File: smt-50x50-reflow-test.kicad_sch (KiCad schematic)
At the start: 86 parts, among them J1 Conn_01x04_Pin, J2 Conn_01x02, J4 USB_C_Receptacle_USB2.0_14P, J8 Conn_01x04_Pin, J9 Conn_01x03_Pin, SW1 SW_Push, SW2 SW_Push, U1 ESP32-C6, U14 TMP117AIDRV, U15 BMP581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

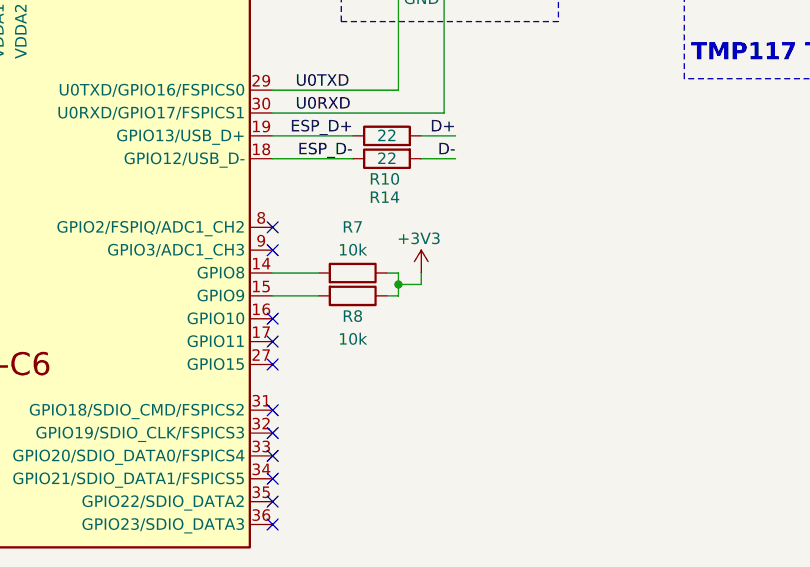
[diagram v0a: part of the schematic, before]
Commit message: schem: add missing i2c net labels
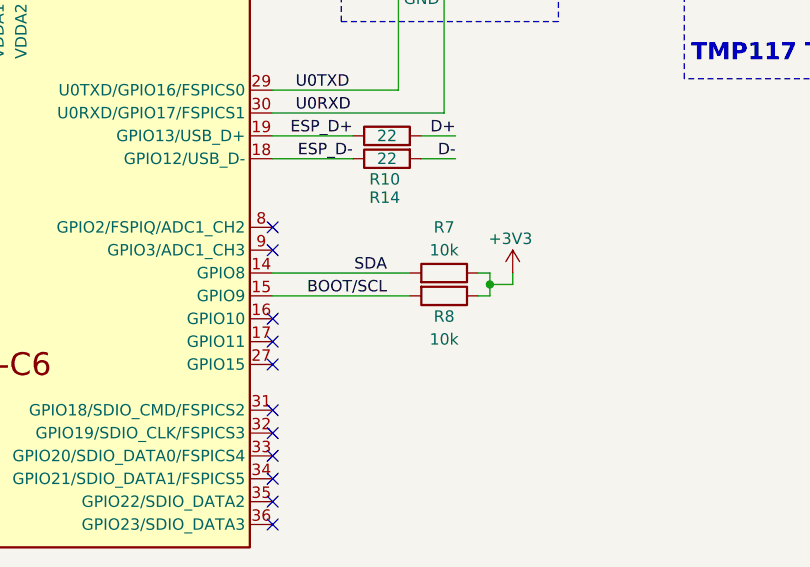
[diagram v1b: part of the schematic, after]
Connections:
- net BOOT/SCL: now also R8.2, U1.15 (GPIO9)
- net SDA: now also R7.2, U1.14 (GPIO8)
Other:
- moved on the sheet: R7, R8
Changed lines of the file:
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@@
 	)
 	(junction
-		(at 152.4 80.01)
+		(at 162.56 80.01)
 		(diameter 0)
 		(color 0 0 0 0)
@@
 	(wire
 		(pts
-			(xy 152.4 81.28) (xy 152.4 80.01)
+			(xy 162.56 81.28) (xy 162.56 80.01)
 		)
 		(stroke
@@
 	(wire
 		(pts
-			(xy 151.13 81.28) (xy 152.4 81.28)
+			(xy 161.29 81.28) (xy 162.56 81.28)
 		)
 		(stroke
@@
 	(wire
 		(pts
-			(xy 152.4 80.01) (xy 152.4 78.74)
+			(xy 162.56 80.01) (xy 162.56 78.74)
 		)
 		(stroke
@@
 	(wire
 		(pts
-			(xy 152.4 78.74) (xy 151.13 78.74)
+			(xy 162.56 78.74) (xy 161.29 78.74)
 		)
 		(stroke
@@
 	(wire
 		(pts
-			(xy 152.4 80.01) (xy 154.94 80.01)
+			(xy 162.56 80.01) (xy 165.1 80.01)
 		)
 		(stroke
@@
 	(wire
 		(pts
-			(xy 138.43 81.28) (xy 143.51 81.28)
+			(xy 138.43 81.28) (xy 153.67 81.28)
 		)
 		(stroke
@@
 	(wire
 		(pts
+			(xy 138.43 78.74) (xy 153.67 78.74)
+		)
+		(stroke
+			(width 0)
+			(type default)
+		)
+	)
+	(wire
+		(pts
 			(xy 41.91 158.75) (xy 44.45 158.75)
 		)
@@
 	(wire
 		(pts
-			(xy 154.94 80.01) (xy 154.94 78.74)
+			(xy 165.1 80.01) (xy 165.1 78.74)
 		)
 		(stroke
@@
 	(wire
 		(pts
-			(xy 143.51 78.74) (xy 138.43 78.74)
-		)
-		(stroke
-			(width 0)
-			(type default)
-		)
-	)
-	(wire
-		(pts
 			(xy 90.17 33.02) (xy 80.01 33.02)
 		)
@@
 		)
 	)
+	(label "BOOT{slash}SCL"
+		(at 151.13 81.28 180)
+		(effects
+			(font
+				(size 1.27 1.27)
+			)
+			(justify right bottom)
+		)
+	)
 	(label "XTAL_P"
 		(at 50.8 180.34 0)
@@
 		)
 	)
+	(label "SDA"
+		(at 151.13 78.74 180)
+		(effects
+			(font
+				(size 1.27 1.27)
+			)
+			(justify right bottom)
+		)
+	)
 	(label "U0RXD"
 		(at 140.97 60.96 0)
@@
 	(symbol
 		(lib_id "power:+3V3")
-		(at 154.94 78.74 0)
+		(at 165.1 78.74 0)
 		(unit 1)
 		(exclude_from_sim no)
@@
 		(dnp no)
 		(property "Reference" "#PWR03"
-			(at 154.94 82.55 0)
+			(at 165.1 82.55 0)
 			(effects
 				(font
@@
 		)
 		(property "Value" "+3V3"
-			(at 154.686 74.93 0)
+			(at 164.846 74.93 0)
 			(effects
 				(font
@@
 		)
 		(property "Footprint" ""
-			(at 154.94 78.74 0)
+			(at 165.1 78.74 0)
 			(effects
 				(font
@@
 		)
 		(property "Datasheet" ""
-			(at 154.94 78.74 0)
+			(at 165.1 78.74 0)
 			(effects
 				(font
@@
 		)
 		(property "Description" "Power symbol creates a global label with name \"+3V3\""
-			(at 154.94 78.74 0)
+			(at 165.1 78.74 0)
 			(effects
 				(font
@@
 	(symbol
 		(lib_id "Device:R")
-		(at 147.32 81.28 270)
+		(at 157.48 81.28 270)
 		(unit 1)
 		(exclude_from_sim no)
@@
 		(dnp no)
 		(property "Reference" "R8"
-			(at 147.32 83.566 90)
+			(at 157.48 83.566 90)
 			(effects
 				(font
@@
 		)
 		(property "Value" "10k"
-			(at 147.32 86.106 90)
+			(at 157.48 86.106 90)
 			(effects
 				(font
@@
 		)
 		(property "Footprint" ""
-			(at 147.32 79.502 90)
+			(at 157.48 79.502 90)
 			(effects
 				(font
@@
 		)
 		(property "Datasheet" "~"
-			(at 147.32 81.28 0)
+			(at 157.48 81.28 0)
 			(effects
 				(font
@@
 		)
 		(property "Description" "Resistor"
-			(at 147.32 81.28 0)
+			(at 157.48 81.28 0)
 			(effects
 				(font
@@
 	(symbol
 		(lib_id "Device:R")
-		(at 147.32 78.74 270)
+		(at 157.48 78.74 270)
 		(mirror x)
 		(unit 1)
@@
 		(dnp no)
 		(property "Reference" "R7"
-			(at 147.32 73.66 90)
+			(at 157.48 73.66 90)
 			(effects
 				(font
@@
 		)
 		(property "Value" "10k"
-			(at 147.32 76.2 90)
+			(at 157.48 76.2 90)
 			(effects
 				(font
@@
 		)
 		(property "Footprint" ""
-			(at 147.32 80.518 90)
+			(at 157.48 80.518 90)
 			(effects
 				(font
@@
 		)
 		(property "Datasheet" "~"
-			(at 147.32 78.74 0)
+			(at 157.48 78.74 0)
 			(effects
 				(font
@@
 		)
 		(property "Description" "Resistor"
-			(at 147.32 78.74 0)
+			(at 157.48 78.74 0)
 			(effects
 				(font

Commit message: schem: add missing footprints
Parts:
- J2: footprint (none) -> Connector_PinHeader_2.54mm:PinHeader_1x02_P2.54mm_Vertical
- R7, R8: footprint (none) -> Resistor_SMD:R_0402_1005Metric
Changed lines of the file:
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@@
 			)
 		)
-		(property "Footprint" ""
+		(property "Footprint" "Connector_PinHeader_2.54mm:PinHeader_1x02_P2.54mm_Vertical"
 			(at 187.96 134.62 0)
 			(effects
@@
 			)
 		)
-		(property "Footprint" ""
+		(property "Footprint" "Resistor_SMD:R_0402_1005Metric"
 			(at 157.48 79.502 90)
 			(effects
@@
 			)
 		)
-		(property "Footprint" ""
+		(property "Footprint" "Resistor_SMD:R_0402_1005Metric"
 			(at 157.48 80.518 90)
 			(effects

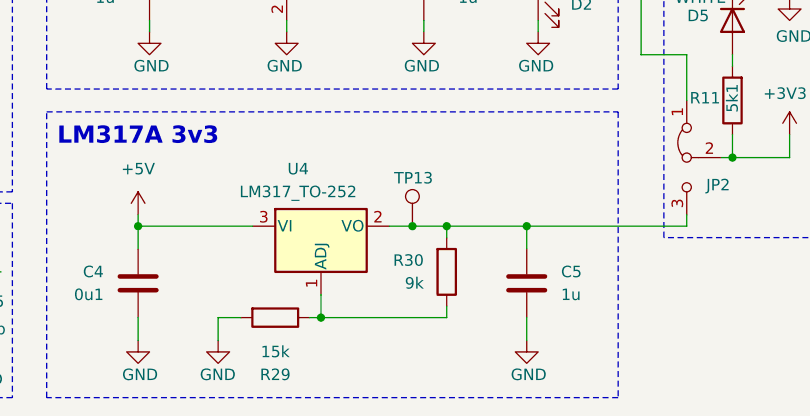
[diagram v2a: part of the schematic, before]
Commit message: schem: add ordering info to BOM
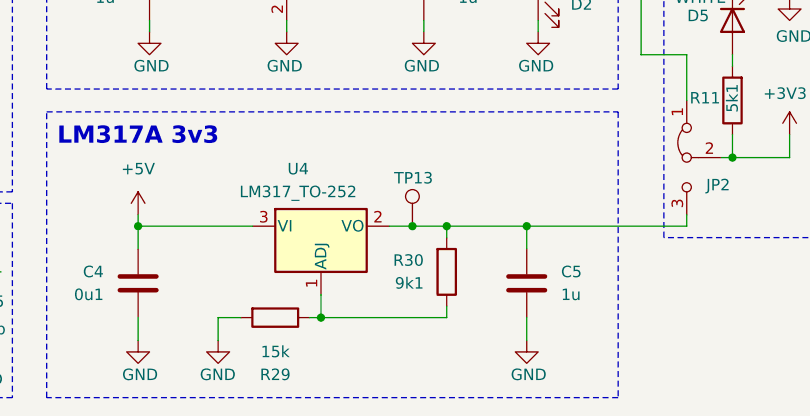
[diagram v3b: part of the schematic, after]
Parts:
- J2: now left out of the parts list
- L2, L4: JLCPCB Part # C412269 -> C77108; Manufacturer Part Number LQW15AN2N7G80D -> LQG15HS2N7S02D
- R29: JLCPCB Part # (none) -> C22809; Manufacturer (none) -> Uniroyal Elec; Manufacturer Part Number (none) -> 0603WAF1502T5E
- R30: value 9k -> 9k1; JLCPCB Part # (none) -> C23260; Manufacturer (none) -> Uniroyal Elec; Manufacturer Part Number (none) -> 0603WAF9101T5E
- R7, R8: JLCPCB Part # (none) -> C25744; Manufacturer (none) -> Uniroyal Elec; Manufacturer Part Number (none) -> 0402WGF1002TCE
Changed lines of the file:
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@@
 		(unit 1)
 		(exclude_from_sim no)
-		(in_bom yes)
+		(in_bom no)
 		(on_board yes)
 		(dnp no)
@@
 			)
 		)
-		(property "JLCPCB Part #" ""
+		(property "JLCPCB Part #" "C22809"
 			(at 110.49 185.42 0)
 			(effects
@@
 			)
 		)
-		(property "Manufacturer" ""
+		(property "Manufacturer" "Uniroyal Elec"
 			(at 110.49 185.42 0)
 			(effects
@@
 			)
 		)
-		(property "Manufacturer Part Number" ""
+		(property "Manufacturer Part Number" "0603WAF1502T5E"
 			(at 110.49 185.42 0)
 			(effects
@@
 			)
 		)
-		(property "Manufacturer Part Number" "LQW15AN2N7G80D"
+		(property "Manufacturer Part Number" "LQG15HS2N7S02D"
 			(at 85.09 22.86 90)
 			(effects
@@
 			)
 		)
-		(property "JLCPCB Part #" "C412269"
+		(property "JLCPCB Part #" "C77108"
 			(at 85.09 22.86 90)
 			(effects
@@
 			)
 		)
+		(property "JLCPCB Part #" "C25744"
+			(at 157.48 81.28 90)
+			(effects
+				(font
+					(size 1.27 1.27)
+				)
+				(hide yes)
+			)
+		)
+		(property "Manufacturer" "Uniroyal Elec"
+			(at 157.48 81.28 90)
+			(effects
+				(font
+					(size 1.27 1.27)
+				)
+				(hide yes)
+			)
+		)
+		(property "Manufacturer Part Number" "0402WGF1002TCE"
+			(at 157.48 81.28 90)
+			(effects
+				(font
+					(size 1.27 1.27)
+				)
+				(hide yes)
+			)
+		)
 		(pin "1"
 		)
@@
 			)
 		)
+		(property "JLCPCB Part #" "C25744"
+			(at 157.48 78.74 90)
+			(effects
+				(font
+					(size 1.27 1.27)
+				)
+				(hide yes)
+			)
+		)
+		(property "Manufacturer" "Uniroyal Elec"
+			(at 157.48 78.74 90)
+			(effects
+				(font
+					(size 1.27 1.27)
+				)
+				(hide yes)
+			)
+		)
+		(property "Manufacturer Part Number" "0402WGF1002TCE"
+			(at 157.48 78.74 90)
+			(effects
+				(font
+					(size 1.27 1.27)
+				)
+				(hide yes)
+			)
+		)
 		(pin "1"
 		)
@@
 			)
 		)
-		(property "Manufacturer Part Number" "LQW15AN2N7G80D"
+		(property "Manufacturer Part Number" "LQG15HS2N7S02D"
 			(at 55.88 39.37 90)
 			(effects
@@
 			)
 		)
-		(property "JLCPCB Part #" "C412269"
+		(property "JLCPCB Part #" "C77108"
 			(at 55.88 39.37 90)
 			(effects
@@
 			)
 		)
-		(property "Value" "9k"
+		(property "Value" "9k1"
 			(at 127 181.6099 0)
 			(effects
@@
 			)
 		)
-		(property "JLCPCB Part #" ""
+		(property "JLCPCB Part #" "C23260"
 			(at 129.54 180.34 90)
 			(effects
@@
 			)
 		)
-		(property "Manufacturer" ""
+		(property "Manufacturer" "Uniroyal Elec"
 			(at 129.54 180.34 90)
 			(effects
@@
 			)
 		)
-		(property "Manufacturer Part Number" ""
+		(property "Manufacturer Part Number" "0603WAF9101T5E"
 			(at 129.54 180.34 90)
 			(effects

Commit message: schem: add title
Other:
- company: (none) -> Rémi Ait-Younes
- title: (none) -> SMT 50x50 reflow test
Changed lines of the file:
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@@
 	(generator_version "9.0")
 	(paper "A4")
+	(title_block
+		(title "SMT 50x50 reflow test")
+		(date "2025-11-15")
+		(rev "01")
+		(company "Rémi Ait-Younes")
+	)
 	(rectangle
 		(start 49.53 172.72)

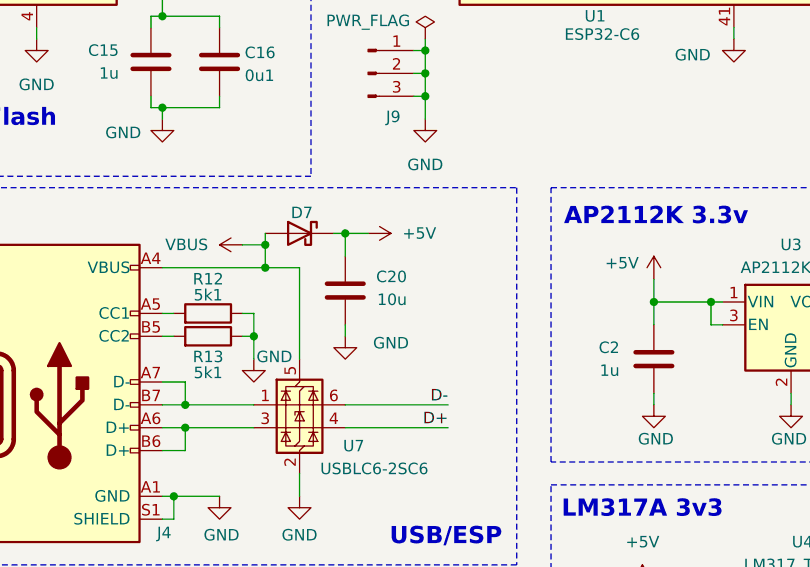
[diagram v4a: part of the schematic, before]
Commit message: schem: add esd protection to usb vbus
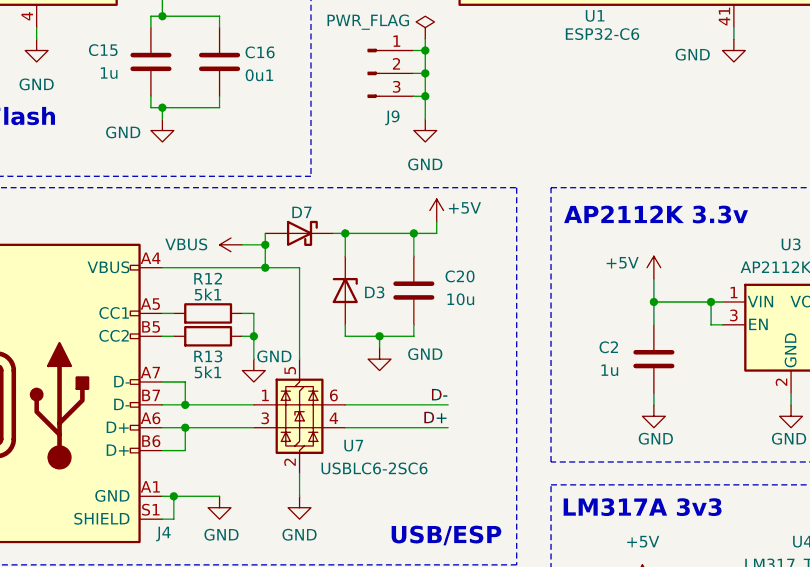
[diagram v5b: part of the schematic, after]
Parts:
- added D3: H5VU10U, Pers:Diode_DFN1006, symbol Pers:H5VU10U
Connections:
- net +5V: now also D3.1 (K)
- net GND: now also D3.2 (A)
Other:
- moved on the sheet: C20
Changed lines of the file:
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@@
 	)
 	(junction
-		(at 62.23 134.62)
+		(at 44.45 156.21)
 		(diameter 0)
 		(color 0 0 0 0)
 	)
 	(junction
-		(at 44.45 156.21)
+		(at 69.85 134.62)
 		(diameter 0)
 		(color 0 0 0 0)
@@
 	)
 	(junction
+		(at 66.04 146.05)
+		(diameter 0)
+		(color 0 0 0 0)
+	)
+	(junction
 		(at 102.87 142.24)
 		(diameter 0)
@@
 	)
 	(junction
+		(at 62.23 134.62)
+		(diameter 0)
+		(color 0 0 0 0)
+	)
+	(junction
 		(at 110.49 44.45)
 		(diameter 0)
@@
 	(wire
 		(pts
+			(xy 72.39 133.35) (xy 72.39 134.62)
+		)
+		(stroke
+			(width 0)
+			(type default)
+		)
+	)
+	(wire
+		(pts
 			(xy 139.7 152.4) (xy 139.7 153.67)
 		)
@@
 	(wire
 		(pts
-			(xy 62.23 134.62) (xy 60.96 134.62)
+			(xy 60.96 134.62) (xy 62.23 134.62)
 		)
 		(stroke
@@
 	(wire
 		(pts
-			(xy 64.77 134.62) (xy 62.23 134.62)
-		)
-		(stroke
-			(width 0)
-			(type default)
-		)
-	)
-	(wire
-		(pts
 			(xy 154.94 36.83) (xy 154.94 44.45)
 		)
@@
 	(wire
 		(pts
+			(xy 62.23 134.62) (xy 69.85 134.62)
+		)
+		(stroke
+			(width 0)
+			(type default)
+		)
+	)
+	(wire
+		(pts
 			(xy 49.53 39.37) (xy 52.07 39.37)
 		)
@@
 	(wire
 		(pts
-			(xy 62.23 146.05) (xy 62.23 144.78)
+			(xy 66.04 147.32) (xy 66.04 146.05)
 		)
 		(stroke
@@
 	(wire
 		(pts
+			(xy 66.04 146.05) (xy 69.85 146.05)
+		)
+		(stroke
+			(width 0)
+			(type default)
+		)
+	)
+	(wire
+		(pts
 			(xy 266.7 64.77) (xy 265.43 64.77)
 		)
@@
 	(wire
 		(pts
+			(xy 62.23 134.62) (xy 62.23 137.16)
+		)
+		(stroke
+			(width 0)
+			(type default)
+		)
+	)
+	(wire
+		(pts
 			(xy 129.54 175.26) (xy 138.43 175.26)
 		)
@@
 	(wire
 		(pts
-			(xy 62.23 134.62) (xy 62.23 137.16)
+			(xy 69.85 134.62) (xy 69.85 137.16)
 		)
 		(stroke
@@
 	(wire
 		(pts
+			(xy 62.23 146.05) (xy 62.23 144.78)
+		)
+		(stroke
+			(width 0)
+			(type default)
+		)
+	)
+	(wire
+		(pts
 			(xy 156.21 175.26) (xy 156.21 173.99)
 		)
@@
 	(wire
 		(pts
+			(xy 62.23 146.05) (xy 66.04 146.05)
+		)
+		(stroke
+			(width 0)
+			(type default)
+		)
+	)
+	(wire
+		(pts
 			(xy 246.38 135.89) (xy 246.38 134.62)
 		)
@@
 	(wire
 		(pts
+			(xy 72.39 134.62) (xy 69.85 134.62)
+		)
+		(stroke
+			(width 0)
+			(type default)
+		)
+	)
+	(wire
+		(pts
 			(xy 67.31 83.82) (xy 72.39 83.82)
 		)
@@
 	(wire
 		(pts
+			(xy 69.85 146.05) (xy 69.85 144.78)
+		)
+		(stroke
+			(width 0)
+			(type default)
+		)
+	)
+	(wire
+		(pts
 			(xy 234.95 34.29) (xy 245.11 34.29)
 		)
@@
 	(symbol
 		(lib_id "Device:C")
-		(at 62.23 140.97 0)
+		(at 69.85 140.97 0)
 		(mirror y)
 		(unit 1)
@@
 		(dnp no)
 		(property "Reference" "C20"
-			(at 69.088 139.446 0)
+			(at 76.708 139.446 0)
 			(effects
 				(font
@@
 		)
 		(property "Value" "10u"
-			(at 69.088 141.986 0)
+			(at 76.708 141.986 0)
 			(effects
 				(font
@@
 		)
 		(property "Footprint" "Capacitor_SMD:C_0402_1005Metric"
-			(at 61.2648 144.78 0)
+			(at 68.8848 144.78 0)
 			(effects
 				(font
@@
 		)
 		(property "Datasheet" "~"
-			(at 62.23 140.97 0)
+			(at 69.85 140.97 0)
 			(effects
 				(font
@@
 		)
 		(property "Description" "Unpolarized capacitor"
-			(at 62.23 140.97 0)
+			(at 69.85 140.97 0)
 			(effects
 				(font
@@
 		)
 		(property "Manufacturer" "Samsung Electro-Mechanics "
-			(at 62.23 140.97 0)
+			(at 69.85 140.97 0)
 			(effects
 				(font
@@
 		)
 		(property "Manufacturer Part Number" "CL05A106MQ5NUNC"
-			(at 62.23 140.97 0)
+			(at 69.85 140.97 0)
 			(effects
 				(font
@@
 		)
 		(property "Basic" "Y"
-			(at 62.23 140.97 0)
+			(at 69.85 140.97 0)
 			(effects
 				(font
@@
 		)
 		(property "JLCPCB Part #" "C15525"
-			(at 62.23 140.97 0)
+			(at 69.85 140.97 0)
 			(effects
 				(font
@@
 	(symbol
 		(lib_id "power:GND")
-		(at 62.23 146.05 0)
+		(at 66.04 147.32 0)
 		(mirror y)
 		(unit 1)
@@
 		(dnp no)
 		(property "Reference" "#PWR045"
-			(at 62.23 152.4 0)
+			(at 66.04 153.67 0)
 			(effects
 				(font
@@
 		)
 		(property "Value" "GND"
-			(at 67.31 146.812 0)
+			(at 71.12 148.082 0)
 			(effects
 				(font
@@
 		)
 		(property "Footprint" ""
-			(at 62.23 146.05 0)
+			(at 66.04 147.32 0)
 			(effects
 				(font
@@
 		)
 		(property "Datasheet" ""
-			(at 62.23 146.05 0)
+			(at 66.04 147.32 0)
 			(effects
 				(font
@@
 		)
 		(property "Description" "Power symbol creates a global label with name \"GND\" , ground"
-			(at 62.23 146.05 0)
+			(at 66.04 147.32 0)
 			(effects
 				(font
@@
 	)
 	(symbol
+		(lib_id "Pers:H5VU10U")
+		(at 62.23 140.97 270)
+		(unit 1)
+		(exclude_from_sim no)
+		(in_bom yes)
+		(on_board yes)
+		(dnp no)
+		(property "Reference" "D3"
+			(at 64.262 141.224 90)
+			(effects
+				(font
+					(size 1.27 1.27)
+				)
+				(justify left)
+			)
+		)
+		(property "Value" "H5VU10U"
+			(at 64.77 142.2399 90)
+			(effects
+				(font
+					(size 1.27 1.27)
+				)
+				(justify left)
+				(hide yes)
+			)
+		)
+		(property "Footprint" "Pers:Diode_DFN1006"
+			(at 57.785 140.97 0)
+			(effects
+				(font
+					(size 1.27 1.27)
+				)
+				(hide yes)
+			)
+		)
+		(property "Datasheet" "https://datasheet.lcsc.com/lcsc/2504101957_hongjiacheng-H5VU10U_C22395519.pdf"
+			(at 62.23 140.97 0)
+			(effects
+				(font
+					(size 1.27 1.27)
+				)
+				(hide yes)
+			)
+		)
+		(property "Description" "-55℃~+155℃ 0.8pF 16V 200nA 55W@8/20us 5A@8/20us 5V 6V ESD IEC 61000-4-2 Unidirectional DFN1006-2L ESD and Surge Protection (TVS/ESD) ROHS"
+			(at 62.23 140.97 0)
+			(effects
+				(font
+					(size 1.27 1.27)
+				)
+				(hide yes)
+			)
+		)
+		(property "Basic" "E"
+			(at 62.23 140.97 90)
+			(effects
+				(font
+					(size 1.27 1.27)
+				)
+				(hide yes)
+			)
+		)
+		(property "JLCPCB Part #" "C22395519"
+			(at 62.23 140.97 90)
+			(effects
+				(font
+					(size 1.27 1.27)
+				)
+				(hide yes)
+			)
+		)
+		(property "Manufacturer" "hongjiacheng"
+			(at 62.23 140.97 90)
+			(effects
+				(font
+					(size 1.27 1.27)
+				)
+				(hide yes)
+			)
+		)
+		(property "Manufacturer Part Number" "H5VU10U"
+			(at 62.23 140.97 90)
+			(effects
+				(font
+					(size 1.27 1.27)
+				)
+				(hide yes)
+			)
+		)
+		(pin "1"
+		)
+		(pin "2"
+		)
+		(instances
+			(project "smt-50x50-reflow-test"
+				(path "/316df49b-410f-46a7-9063-0920c2d0517b"
+					(reference "D3")
+					(unit 1)
+				)
+			)
+		)
+	)
+	(symbol
 		(lib_id "Pers:BMP581")
 		(at 262.89 80.01 0)
@@
 	(symbol
 		(lib_id "power:+5V")
-		(at 64.77 134.62 270)
-		(mirror x)
+		(at 72.39 133.35 0)
+		(mirror y)
 		(unit 1)
 		(exclude_from_sim no)
@@
 		(on_board yes)
 		(dnp no)
-		(fields_autoplaced yes)
 		(property "Reference" "#PWR044"
-			(at 60.96 134.62 0)
+			(at 72.39 137.16 0)
 			(effects
 				(font
@@
 		)
 		(property "Value" "+5V"
-			(at 68.58 134.6199 90)
+			(at 75.438 131.826 0)
 			(effects
 				(font
 					(size 1.27 1.27)
 				)
-				(justify left)
 			)
 		)
 		(property "Footprint" ""
-			(at 64.77 134.62 0)
+			(at 72.39 133.35 0)
 			(effects
 				(font
@@
 		)
 		(property "Datasheet" ""
-			(at 64.77 134.62 0)
+			(at 72.39 133.35 0)
 			(effects
 				(font
@@
 		)
 		(property "Description" "Power symbol creates a global label with name \"+5V\""
-			(at 64.77 134.62 0)
+			(at 72.39 133.35 0)
 			(effects
 				(font

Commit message: schem: run and fix ERC
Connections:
- net BMP_INT1: now also U1.34 (GPIO21/SDIO_DATA1/FSPICS5)
- net TMP117_ALERT: now also U1.35 (GPIO22/SDIO_DATA2)
- net TMP117_ALERT2: now also U1.36 (GPIO23/SDIO_DATA3)
- net XTAL_32K_N: no longer names the net of U1.7 (GPIO1/XTAL_32K_N/ADC1_CH1)
- net XTAL_32K_P: no longer names the net of U1.6 (GPIO0/XTAL_32K_P/ADC1_CH0)
- no-connect marks 11 -> 10

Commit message: schem: add smol area
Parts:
- added C3: 2k2, Capacitor_SMD:C_0201_0603Metric, symbol Device:C
- added D4: ORANGE, LED_SMD:LED_0201_0603Metric, symbol Device:LED
- added J3, J5, J6, J7: Conn_01x01, TestPoint:TestPoint_Pad_D1.0mm, symbol Connector_Generic:Conn_01x01
- added R17, R18: 5k1, Resistor_SMD:R_0201_0603Metric, symbol Device:R
- added R19: 10k, Resistor_SMD:R_0201_0603Metric, symbol Device:R
- added R20: 24k, Resistor_SMD:R_0201_0603Metric, symbol Device:R
- added R21: 70, Resistor_SMD:R_0201_0603Metric, symbol Device:R
- added R22: 39k, Resistor_SMD:R_0201_0603Metric, symbol Device:R
- added R23: 20k, Resistor_SMD:R_01005_0402Metric, symbol Device:R
- added R24: 750, Resistor_SMD:R_01005_0402Metric, symbol Device:R
- added R25: 1k33, Resistor_SMD:R_01005_0402Metric, symbol Device:R
- added R26: 4k3, Resistor_SMD:R_01005_0402Metric, symbol Device:R
- added TP1: TestPoint, TestPoint:TestPoint_Pad_D2.0mm, symbol Connector:TestPoint
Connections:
- net GND: now also C3.2, D4.1 (K)
- net at U1.31 (GPIO18/SDIO_CMD/FSPICS2): now also R17.1
- net at U1.32 (GPIO19/SDIO_CLK/FSPICS3): now also R18.1
- new net: C3.1, R18.2, TP1.1
- new net: J3.1 (Pin_1), R19.1, R20.1, R21.1, R22.1
- new net: J5.1 (Pin_1), R19.2, R20.2, R21.2, R22.2
- new net: J6.1 (Pin_1), R23.1, R24.1, R25.1, R26.1
- new net: J7.1 (Pin_1), R23.2, R24.2, R25.2, R26.2
- new net: D4.2 (A), R17.2
- no-connect marks 10 -> 8
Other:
- note added: "01005"
- note added: "0201"
- note added: "Smol area"
